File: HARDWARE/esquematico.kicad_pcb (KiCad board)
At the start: 2 copper layers, 53 parts, among them J1 Screw_Terminal_01x02, J10 LCD I2C, J12 Screw_Terminal_01x02, J13 Screw_Terminal_01x02, J14 Screw_Terminal_01x02, J15 Screw_Terminal_01x02, J2 Screw_Terminal_01x02, J3 Screw_Terminal_01x02, J4 Screw_Terminal_01x02, J5 Screw_Terminal_01x02, J6 PINERA, K1 G6AU, K2 G6AU, K3 G6AU, K4 G6AU, Q1 2N7000, Q2 2N7000, Q3 2N7000, Q4 2N7000, SW1 SW_SPST, U1 PC817, U2 ESP32-DEVKITC-32D, U3 L7805, U4 PC817, U5 PC817, U6 PC817

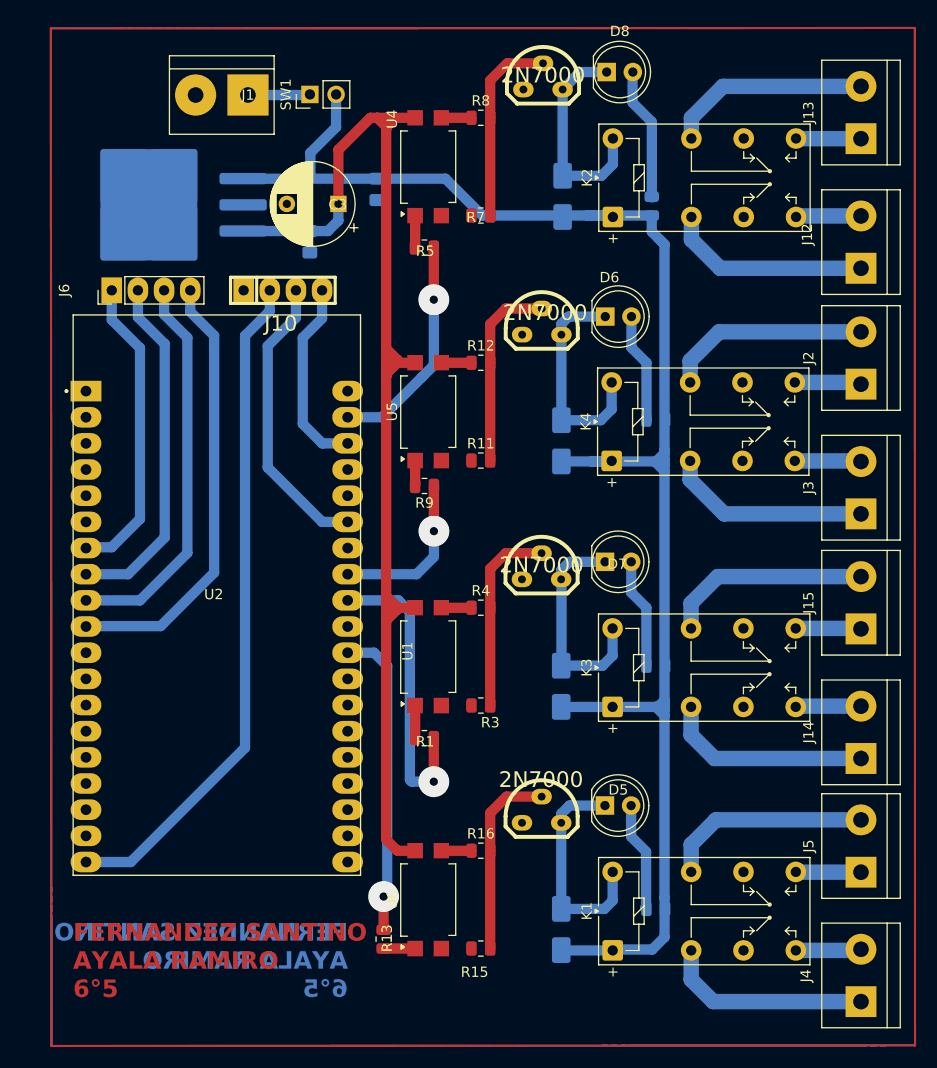
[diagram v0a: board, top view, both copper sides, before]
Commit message: cambie el esp32 de 38 pines por uno de 30
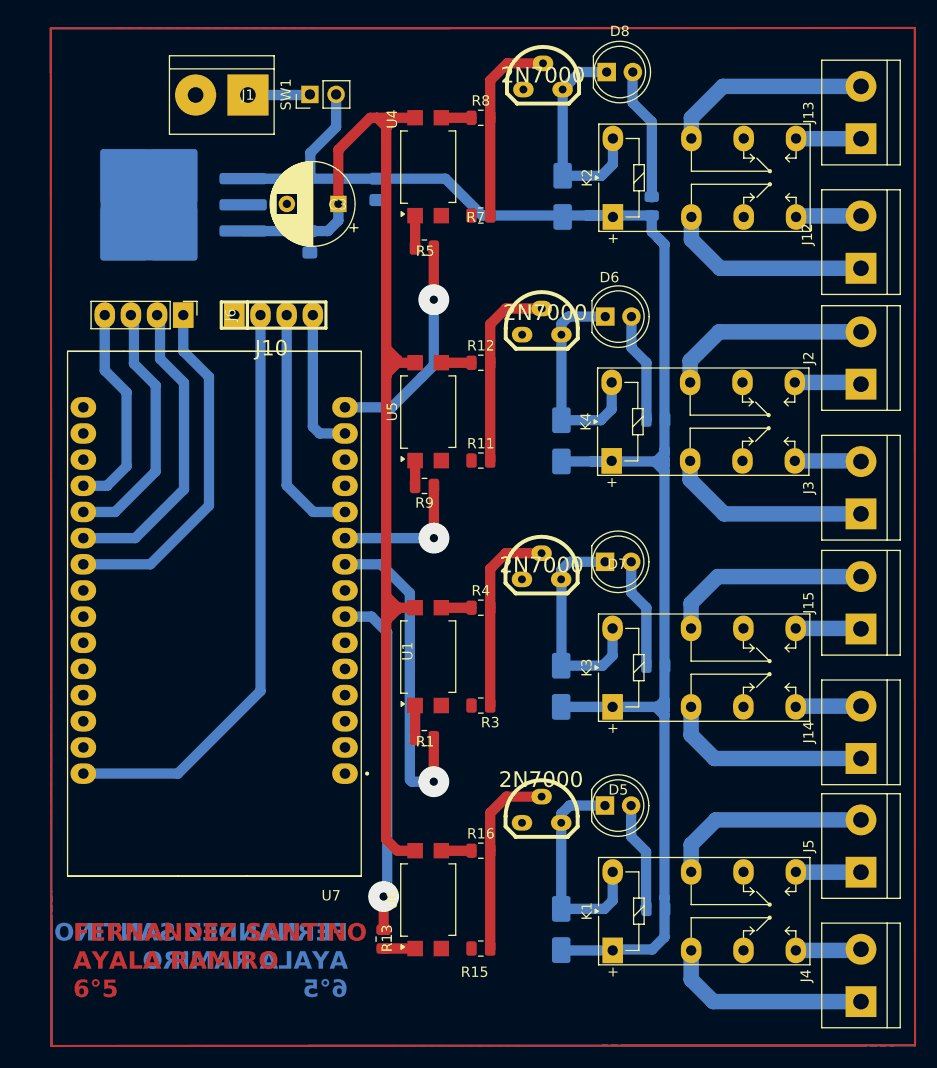
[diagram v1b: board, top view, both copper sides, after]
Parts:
- removed U2: ESP32-DEVKITC-32D, nueva huella esp32:MODULE_ESP32-DEVKITC-32D
- added U7: ESP32-DEVKIT-30pin, MixLib-main:MODULE_ESP32_DEVKIT_V1, F.Cu at (89.0, 141.0)
- J6: value PINERA -> PINERA
- moved J6 7.34 mm to (86.0, 112.0), turned to -90 degrees
- moved J10 2.56 mm to (94.8, 112.0)
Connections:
- J6 pad 3: GPIO25 -> GPIO35
- J6 pad 4: GPIO26 -> GPIO34
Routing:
- net GPIO26: track 43.0 -> 0.00 mm
- net GPIO25: track 38.4 -> 0.00 mm
- net GPIO35: track 0.00 -> 25.0 mm
- net GPIO34: track 0.00 -> 20.9 mm
- net 5V: track 65.4 -> 57.0 mm
- net SCL: track 19.3 -> 14.2 mm
- net SDA: track 28.3 -> 23.3 mm
- net GPIO33: track 34.2 -> 29.7 mm
- net GPIO32: track 29.7 -> 33.8 mm
- net GPIO17: track 30.9 -> 34.5 mm
- net GPIO18: track 29.5 -> 32.3 mm
- net GPIO19: track 16.7 -> 14.3 mm
